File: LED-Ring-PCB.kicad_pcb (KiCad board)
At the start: 2 copper layers, 88 x 88 mm, 34 parts, among them J1 Conn_01x04, J2 Conn_01x04

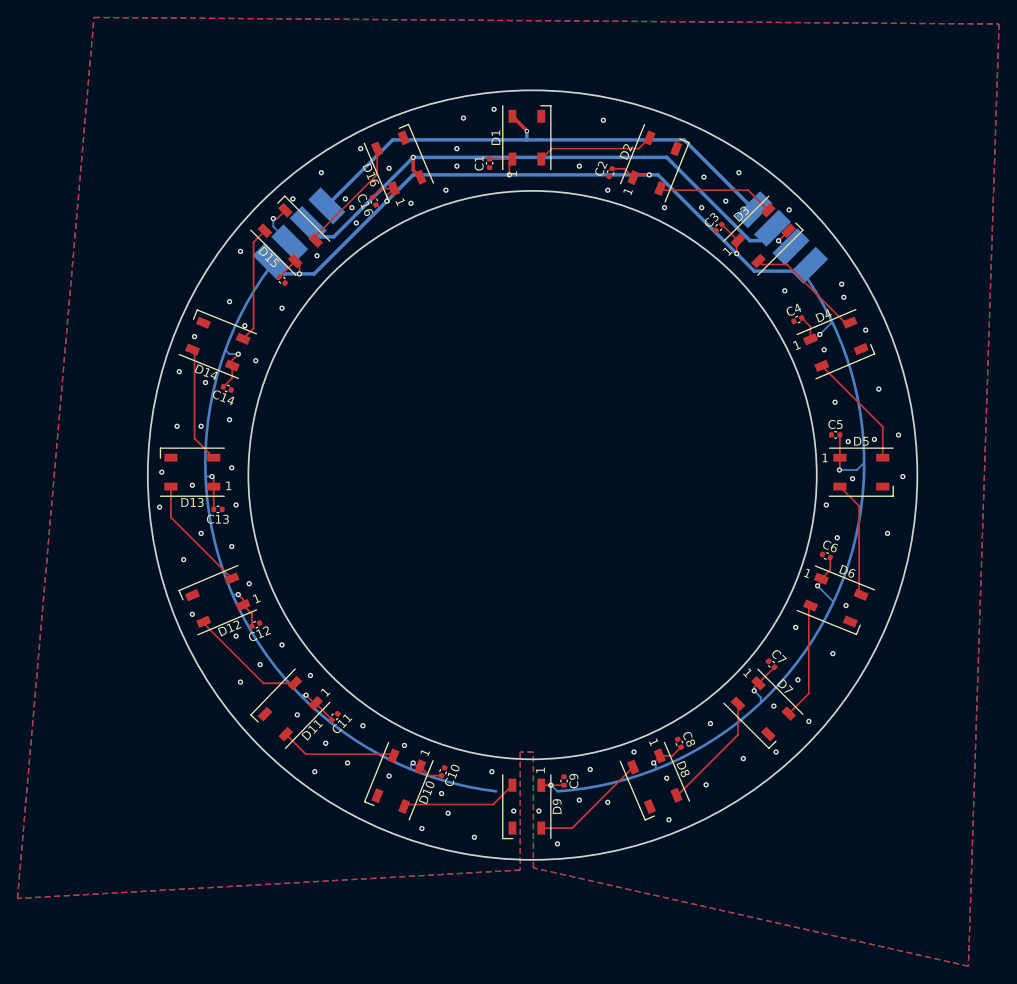
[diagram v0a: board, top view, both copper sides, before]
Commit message: Updated capacitor-packages from 0402 to 0603
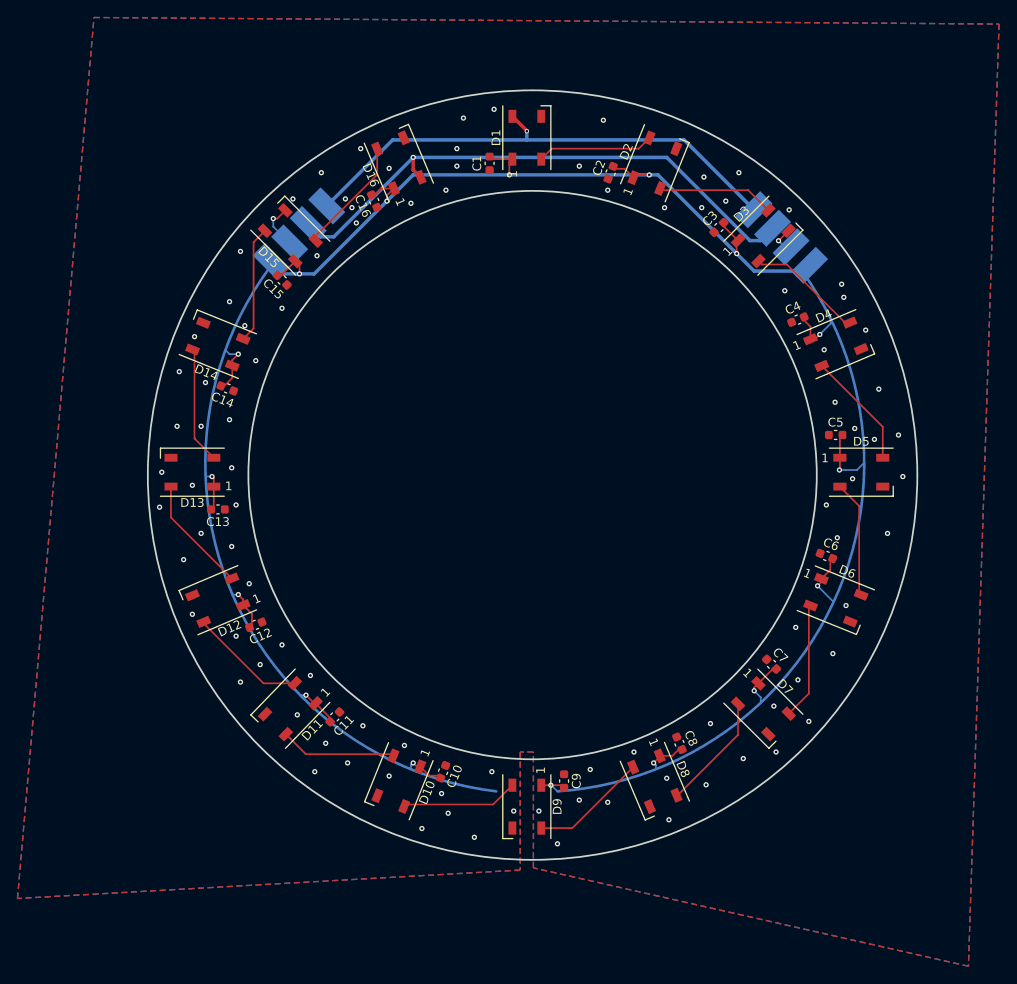
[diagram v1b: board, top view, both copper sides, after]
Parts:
- C1, C10, C11, C12, C13, C14, C15, C16, C2, C3, C4, C5, C6, C7, C8, C9: footprint Capacitor_SMD:C_0402_1005Metric -> Capacitor_SMD:C_0603_1608Metric

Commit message: Added Pritings for the numbers. (Rev. 2)
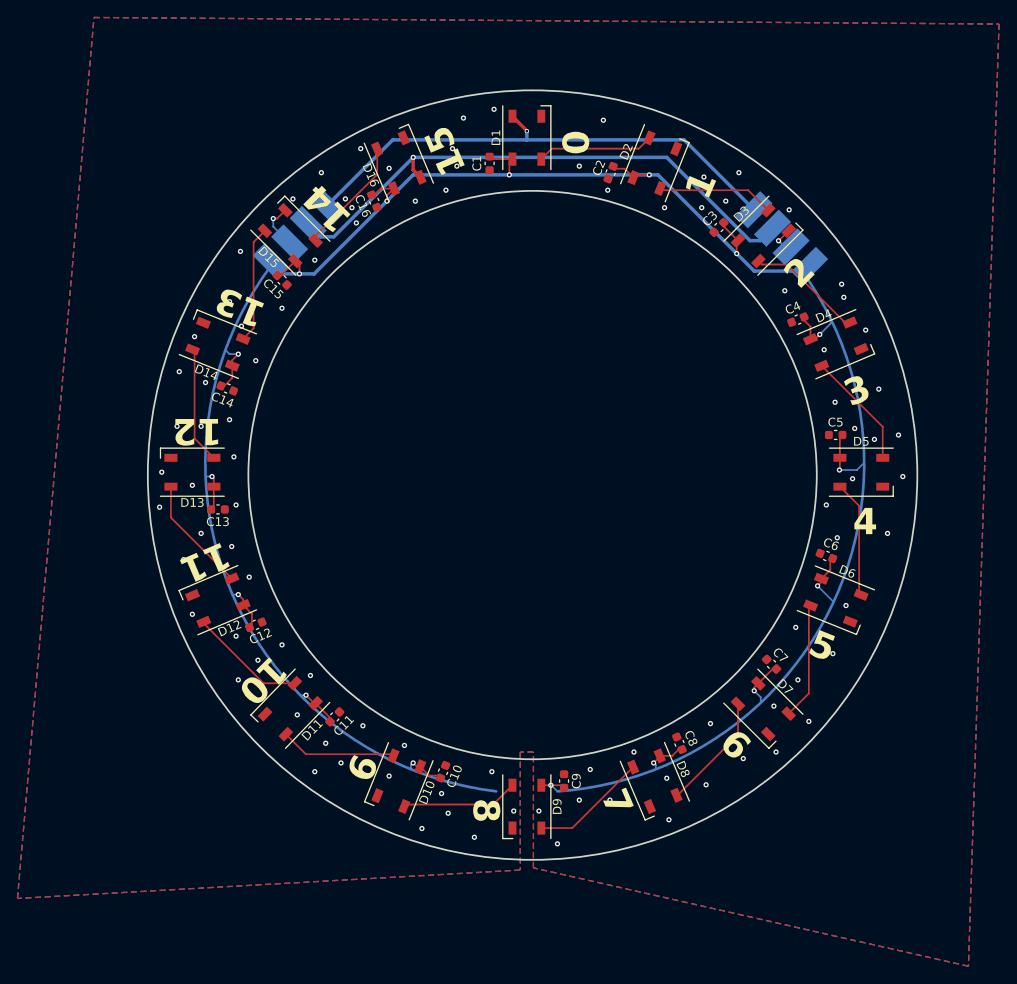
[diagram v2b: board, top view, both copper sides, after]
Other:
- board text added: "0"
- board text added: "1"
- board text added: "10"
- board text added: "11"
- board text added: "12"
- board text added: "13"
- board text added: "14"
- board text added: "15"
- board text added: "2"
- board text added: "3"
- board text added: "4"
- board text added: "5"
- board text added: "6"
- board text added: "7"
- board text added: "8"
- board text added: "9"
- board text added: "LED-Brillen-Ring rev. 2"
- board text removed: "LED-Brillen-Ring rev. 1"
